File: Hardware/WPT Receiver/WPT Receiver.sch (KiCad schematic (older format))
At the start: 18 parts

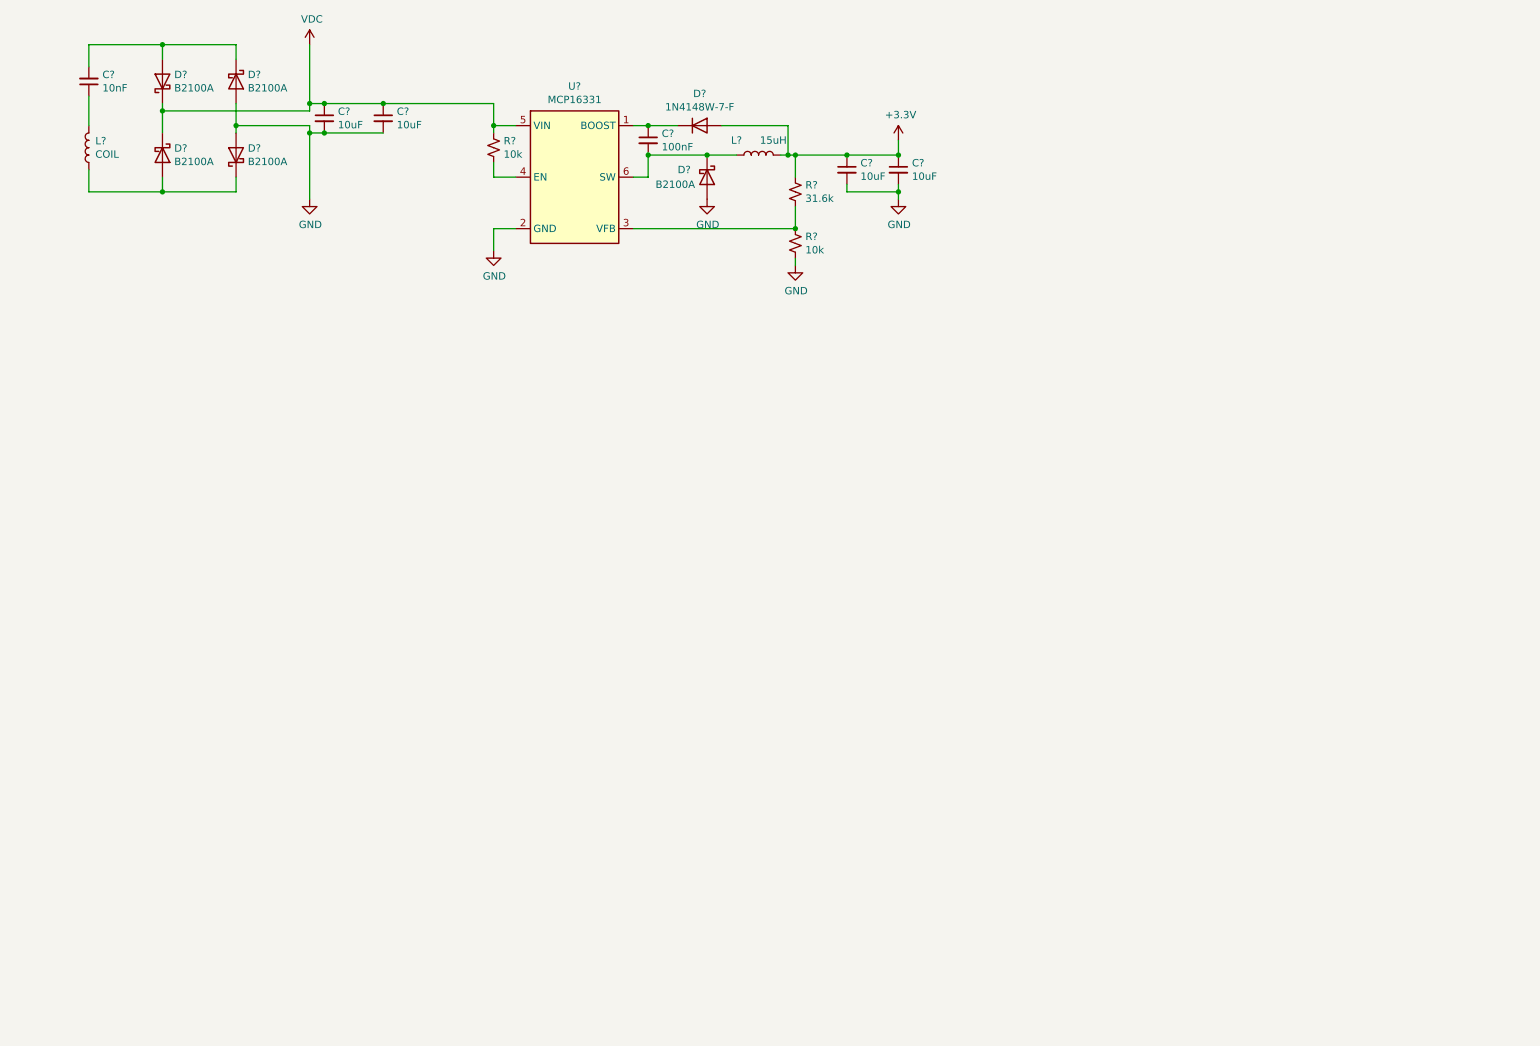
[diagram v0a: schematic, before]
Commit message: updated title block parameters for both schematic. In receiver, modified symbol of STM32, added to schematic and also added crystal, decoupling caps, and buttons
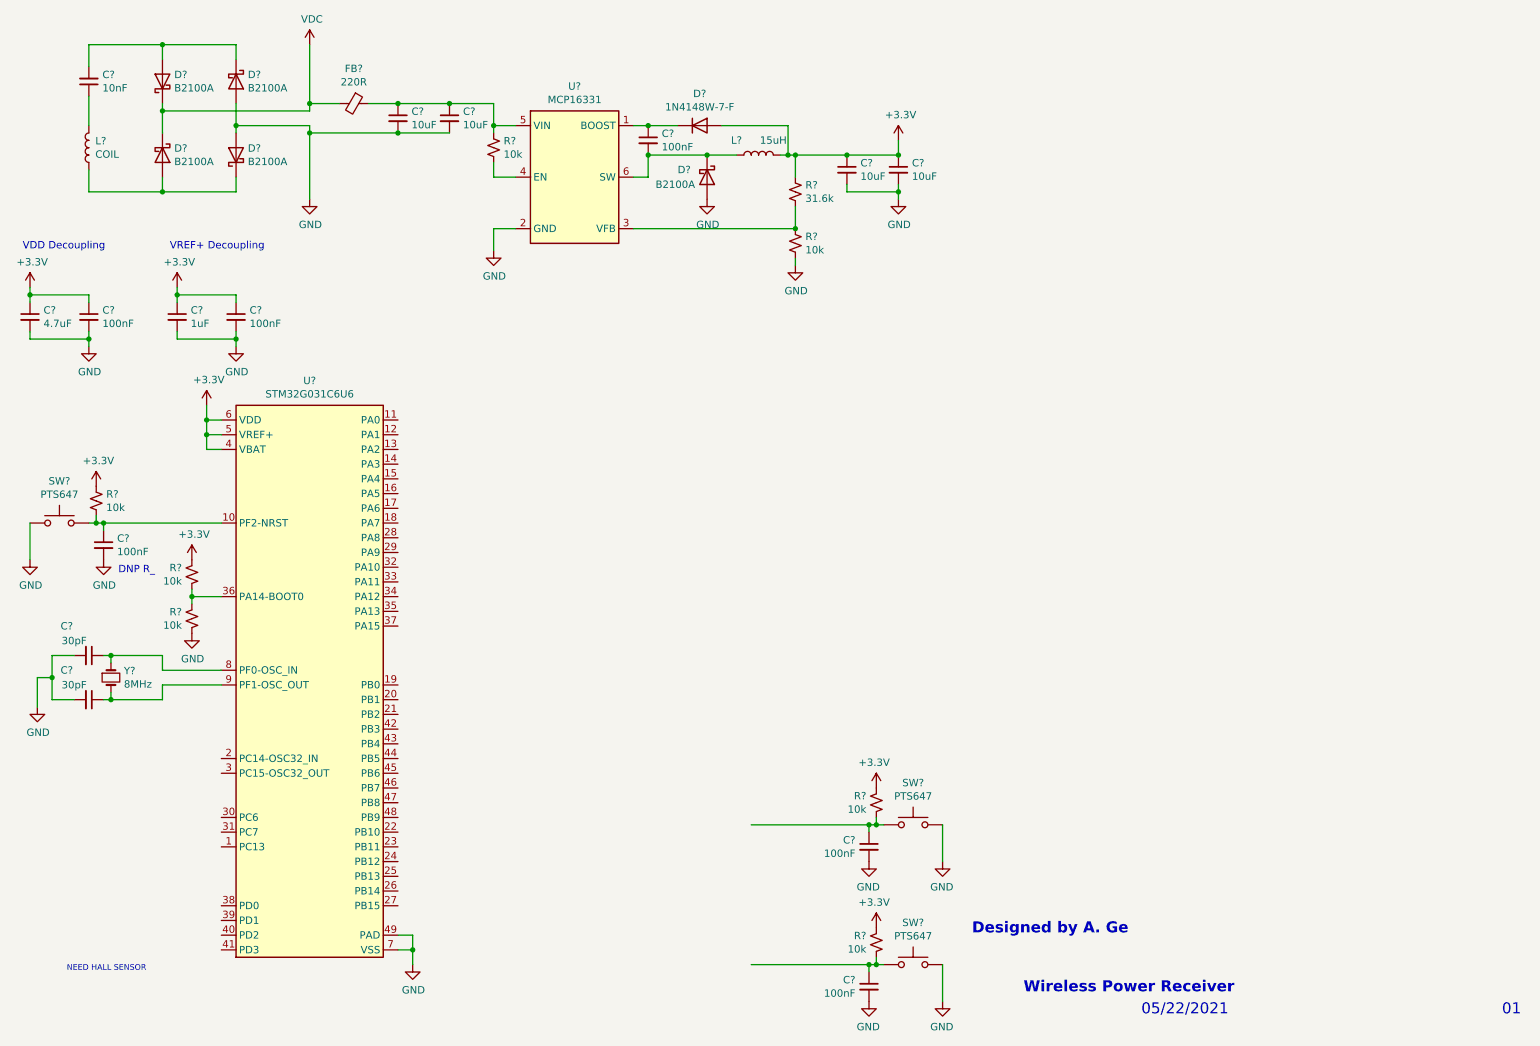
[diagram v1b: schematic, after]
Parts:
- added C? (x2): 30pF, symbol Device:C_Small
- added C? (x5): 100nF, symbol Device:C_Small
- added C?: 4.7uF, symbol Device:C_Small
- added C?: 1uF, symbol Device:C_Small
- added FB?: 220R, symbol Device:Ferrite_Bead_Small
- added R? (x5): 10k, symbol Device:R_Small_US
- added SW? (x3): PTS647, MyParts:PTS647, symbol WPT_Project_Parts:PTS647
- added U?: STM32G031C6U6, Package_DFN_QFN:QFN-48-1EP_7x7mm_P0.5mm_EP5.6x5.6mm, symbol WPT_Project_Parts:STM32G031C6U6
- added Y?: 8MHz, symbol Device:Crystal_Small
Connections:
- net +3V3: now also C?.1, C?.1, C?.1, C?.1, R?.1, R?.1, R?.1, R?.2, U?.4 (VBAT), U?.5 (VREF+), U?.6 (VDD)
- net GND: now also C?.2, C?.2, C?.2, C?.2, C?.2, C?.2, C?.2, C?.2, C?.2, R?.1, SW?.1, SW?.1, SW?.1, U?.49 (PAD), U?.7 (VSS)
- net VDC: now also FB?.2; no longer C?.1, C?.1, R?.1, U?.5 (VIN)
- new net: C?.1, C?.1, FB?.1, R?.1, U?.5 (VIN)
- new net: C?.1, R?.2, SW?.2, U?.10 (PF2-NRST)
- new net: R?.1, R?.2, U?.36 (PA14-BOOT0)
- new net: C?.1, U?.8 (PF0-OSC_IN), Y?.1
- new net: C?.1, U?.9 (PF1-OSC_OUT), Y?.2
- new net: C?.1, R?.2, SW?.2 (x2)
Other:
- note added: "01"
- note added: "05/22/2021\n"
- note added: "DNP R_"
- note added: "Designed by A. Ge\n"
- note added: "NEED HALL SENSOR"
- note added: "VDD Decoupling"
- note added: "VREF+ Decoupling"
- note added: "Wireless Power Receiver\n"
- moved on the sheet: C?

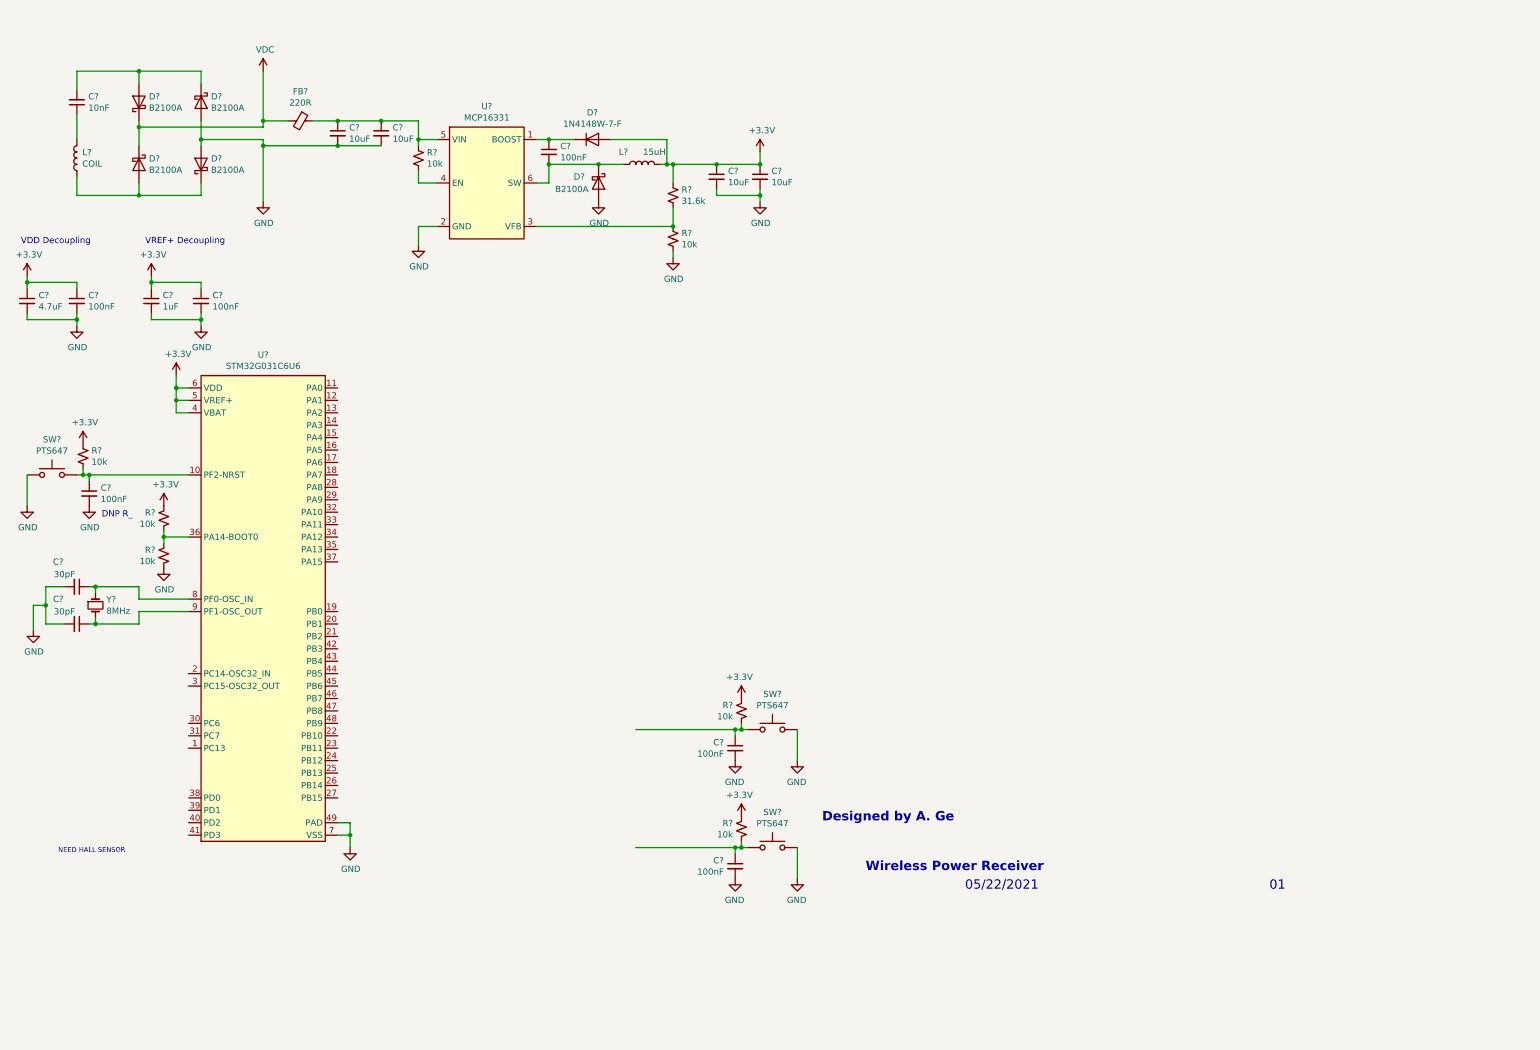
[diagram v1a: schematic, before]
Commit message: Added placeholder text for remaining parts of board (hall sensor, temp sensor, current sense, LEDs, etc.)
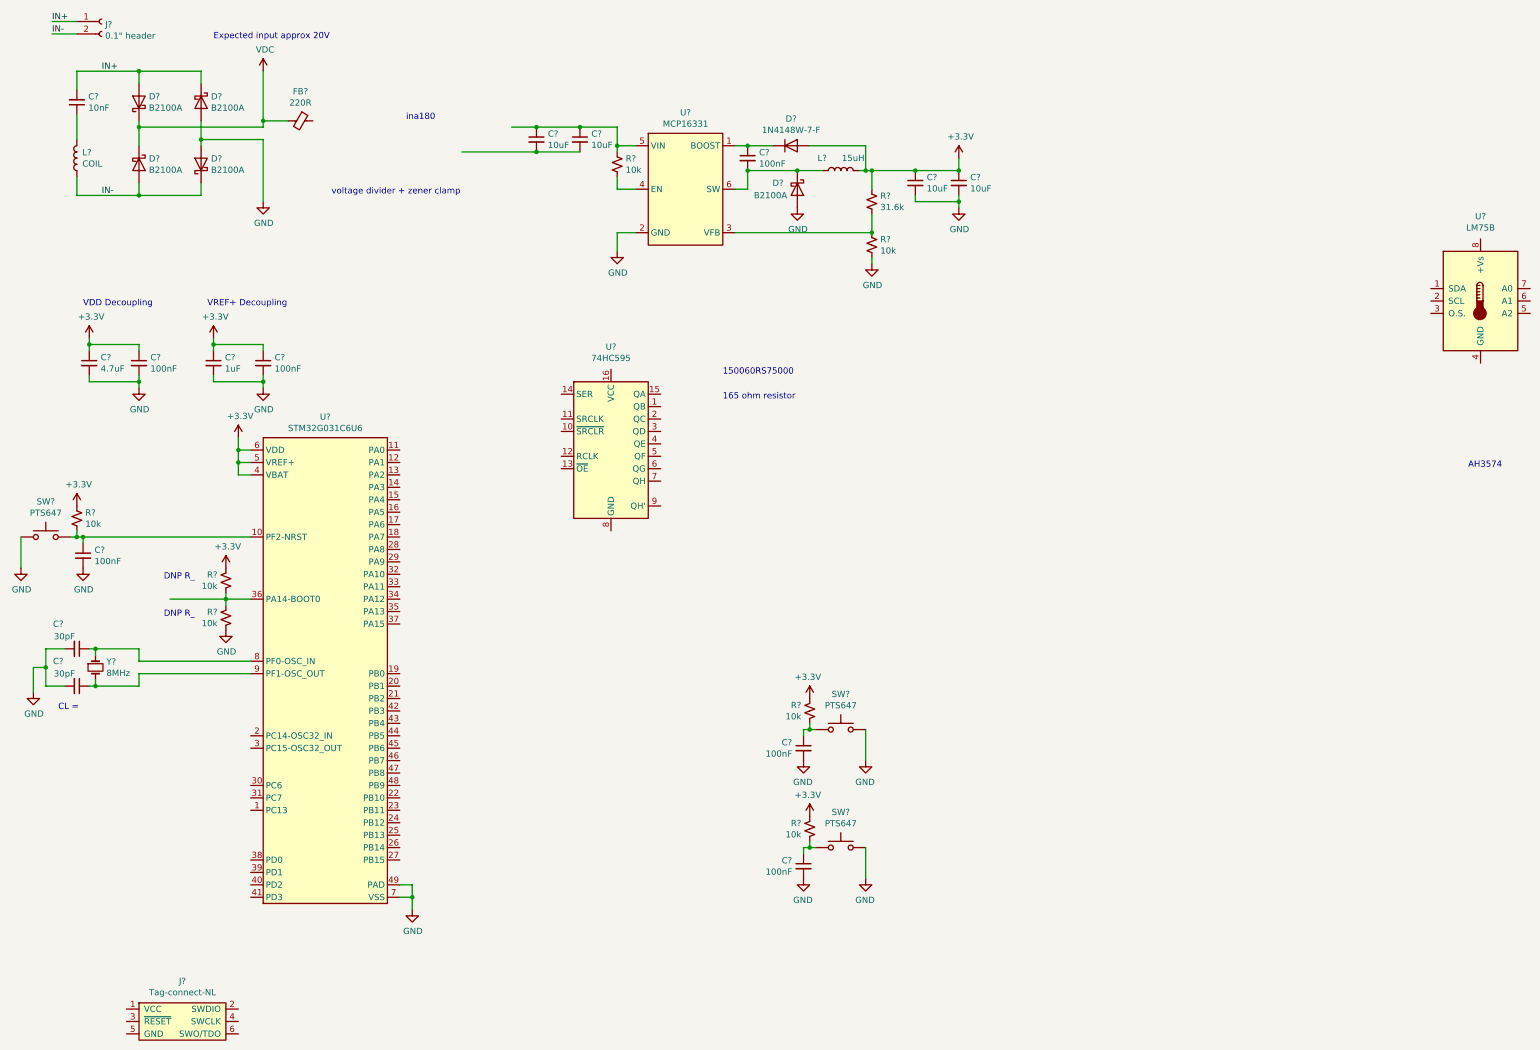
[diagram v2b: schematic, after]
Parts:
- added J?: 0.1\" header, symbol Connector:Conn_01x02_Female
- added J?: Tag-connect-NL, Tag-connect:TC2030-IDC-NL-FP, symbol Tag-connect:Tag-connect-NL
- added U?: LM75B, symbol Sensor_Temperature:LM75B
- added U?: 74HC595, symbol 74xx:74HC595
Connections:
- net GND: no longer C?.2, C?.2
- net at C?.1, C?.1, R?.1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: no longer FB?.1
- net IN+: now reaches C?.2, D?.1 (K), D?.2 (A)
- net IN+: now also J?.1 (Pin_1)
- net IN-: now reaches D?.1 (K), D?.2 (A), L?.1
- net IN-: now also J?.2 (Pin_2)
- new net: C?.2, C?.2
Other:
- note added: "150060RS75000"
- note added: "165 ohm resistor\n"
- note added: "AH3574"
- note added: "CL ="
- note added: "Expected input approx 20V"
- note added: "ina180"
- note added: "voltage divider + zener clamp"
- note removed: "01"
- note removed: "05/22/2021\n"
- note removed: "Designed by A. Ge\n"
- note removed: "NEED HALL SENSOR"
- note removed: "Wireless Power Receiver\n"
- moved on the sheet: C?, D?, L?, R?, SW?, U?, Y?

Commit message: Created symbols for INA180 and Hall sensor. Added to schematic and implemented supporting circuitry. Added background color to old tag connect symbol
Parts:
- added C? (x3): 100nF, symbol Device:C_Small
- added R?: 60m, symbol Device:R_Small_US
- added R? (x3): 10k, symbol Device:R_Small_US
- added R?: 100k, symbol Device:R_Small_US
- added R?: 0, symbol Device:R_Small_US
- added U?: INA180A3, Package_TO_SOT_SMD:SOT-23-5, symbol WPT_Project_Parts:INA180A3
- added U?: AH3574-P, Package_TO_SOT_THT:TO-92Flat, symbol WPT_Project_Parts:AH3574-P
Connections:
- net +3V3: now also J?.1 (VCC), U?.8 (+Vs), C?.1, C?.1, C?.1, R?.1, R?.1, R?.1, R?.2, U?.1 (VDD), U?.5 (VS)
- net GND: now also C?.2, C?.2, J?.5 (GND), U?.4 (GND), U?.5 (A2), U?.6 (A1), U?.7 (A0), C?.2, C?.2, C?.2, U?.2 (GND), U?.2 (GND)
- net VDC: now also C?.1, C?.1, R?.1, U?.5 (VIN), R?.2, U?.4 (IN-); no longer D?.1 (K), D?.1 (K), FB?.2
- net SWDIO: now reaches U?.35 (PA13)
- net SWDIO: now also J?.2 (SWDIO)
- net SWCLK: now reaches R?.1, R?.2, U?.36 (PA14-BOOT0)
- net SWCLK: now also J?.4 (SWCLK)
- net at FB?.1: now also R?.1, U?.3 (IN+)
- net at J?.3 (~RESET): now also R?.2
- net SDA: now reaches U?.1 (SDA)
- net SDA: now also R?.2
- net SCL: now reaches U?.2 (SCL)
- net SCL: now also R?.2
- net TEMP_INT: now reaches U?.3 (O.S.)
- net TEMP_INT: now also R?.2
- new net: D?.1 (K), D?.1 (K), FB?.2
- new net HALL_INT: R?.1, U?.3 (OUT)
- new net ISENSE: U?.1 (OUT)
- no-connect marks 0 -> 1
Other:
- note added: "60mΩ * 500mA max = 30mV\n30mV * 100V/V gain = 3V"
- note added: "I2C address: 0x48"
- note added: "TO DO LIST\nCreate symbol for hall sense, current sense\nImport STM32 pinout\nCreate circuits for smaller peripherals\nCreate and duplicate LED circuits\nAdd in extra headers\nThink about adding more capacitance/protection\nClean up"
- note removed: "AH3574"
- note removed: "ina180"
- moved on the sheet: C?, D?, FB?, J?, L?, R?, SW?, U?, Y?

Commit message: Added most of pinout for STM32G0, as well as measurement circuit for voltage sense. Added implementation for one shift reg.
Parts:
- added C?: 100nF, symbol Device:C_Small
- added D? (x8): RED, symbol Device:LED_ALT
- added D?: 3.3V, symbol Device:D_Zener_Small
- added R? (x8): 165, symbol Device:R_Small_US
- added R?: 100k, symbol Device:R_Small_US
- added R? (x2): 10k, symbol Device:R_Small_US
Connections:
- net +3V3: now also U?.16 (VCC), C?.1, D?.2 (A), D?.2 (A), D?.2 (A), D?.2 (A), D?.2 (A), D?.2 (A), D?.2 (A), D?.2 (A)
- net GND: now also U?.8 (GND), C?.2, D?.2 (A), R?.2, R?.2
- net HALL_INT: now also U?.39 (PD1)
- net ISENSE: now also U?.12 (PA1)
- net SCL: now also U?.29 (PA9)
- net SDA: now also U?.32 (PA10)
- net VDC: now also R?.1
- net RST: now reaches C?.1, R?.2, SW?.2, U?.10 (PF2-NRST)
- net RST: now also R?.1
- net USER_BTN1: now reaches U?.11 (PA0)
- net VSENSE: now reaches U?.13 (PA2)
- net VSENSE: now also D?.1 (K), R?.1, R?.1, R?.2
- net RCLK: now reaches U?.15 (PA4)
- net RCLK: now also U?.12 (RCLK)
- net SRCLK: now reaches U?.16 (PA5)
- net SRCLR: now reaches U?.17 (PA6)
- net SRCLR: now also U?.10 (~SRCLR)
- net SER: now reaches U?.18 (PA7)
- net SR_EN: now reaches U?.19 (PB0)
- net SR_EN: now also U?.13 (~OE)
- net DEBUG_RX: now reaches U?.22 (PB10)
- net DEBUG_TX: now reaches U?.23 (PB11)
- net at U?.1 (QB): now also R?.2
- net at U?.15 (QA): now also R?.2
- net at U?.2 (QC): now also R?.2
- net at U?.3 (QD): now also R?.2
- net at U?.4 (QE): now also R?.2
- net at U?.5 (QF): now also R?.2
- net at U?.6 (QG): now also R?.2
- net at U?.7 (QH): now also R?.2
- new net: D?.1 (K), R?.1 (x8)
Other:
- note added: "LED: Wurth 150060RS75000"
- note added: "SPI1_MOSI"
- note added: "SPI1_SCK"
- note removed: "150060RS75000"
- moved on the sheet: C?, J?, R?, SW?, U?
